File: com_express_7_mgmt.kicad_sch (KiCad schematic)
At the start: 40 parts, among them J1 Plug_Bus_CE7_EPT_401-51501-51, Q1 BSS138-7-F, Q2 BSS138-7-F, SW1 SW_1-1825027-1_THT, SW2 SW_1-1825027-1_THT, U30 MAX16150A_SOT, U31 74AUP2G132, U32 TPS3840PL30DBVR, U33 74AUP2G132

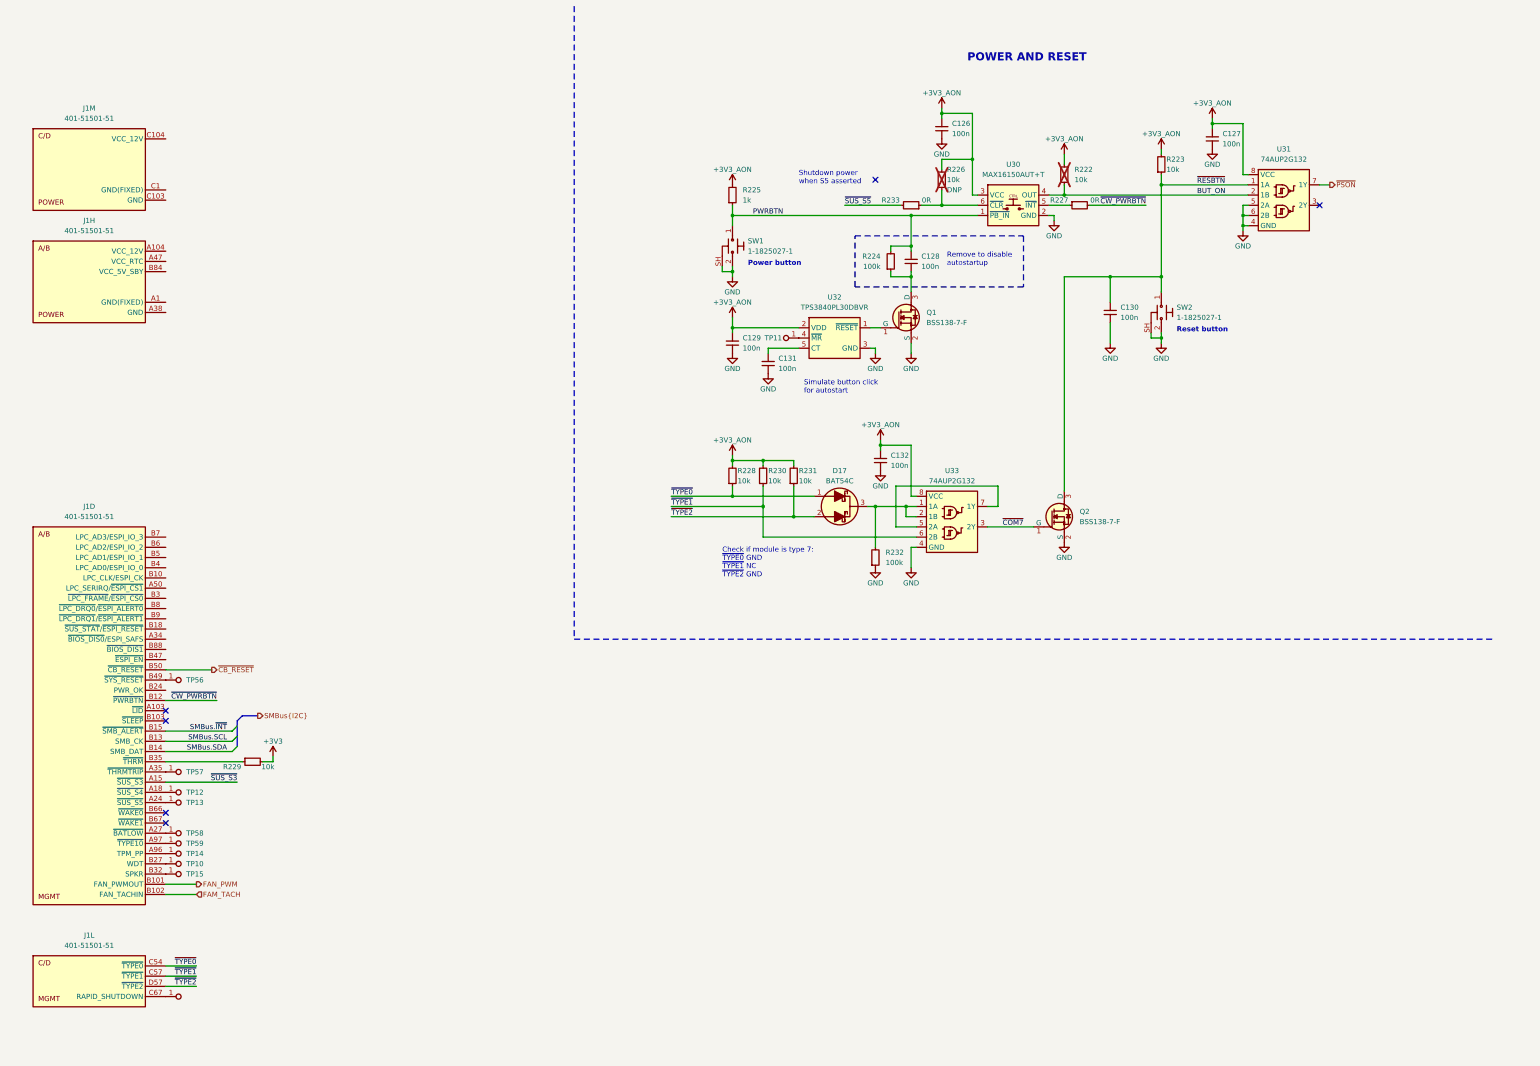
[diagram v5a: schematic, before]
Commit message: [#57905] Add MAFS carrier BIOS
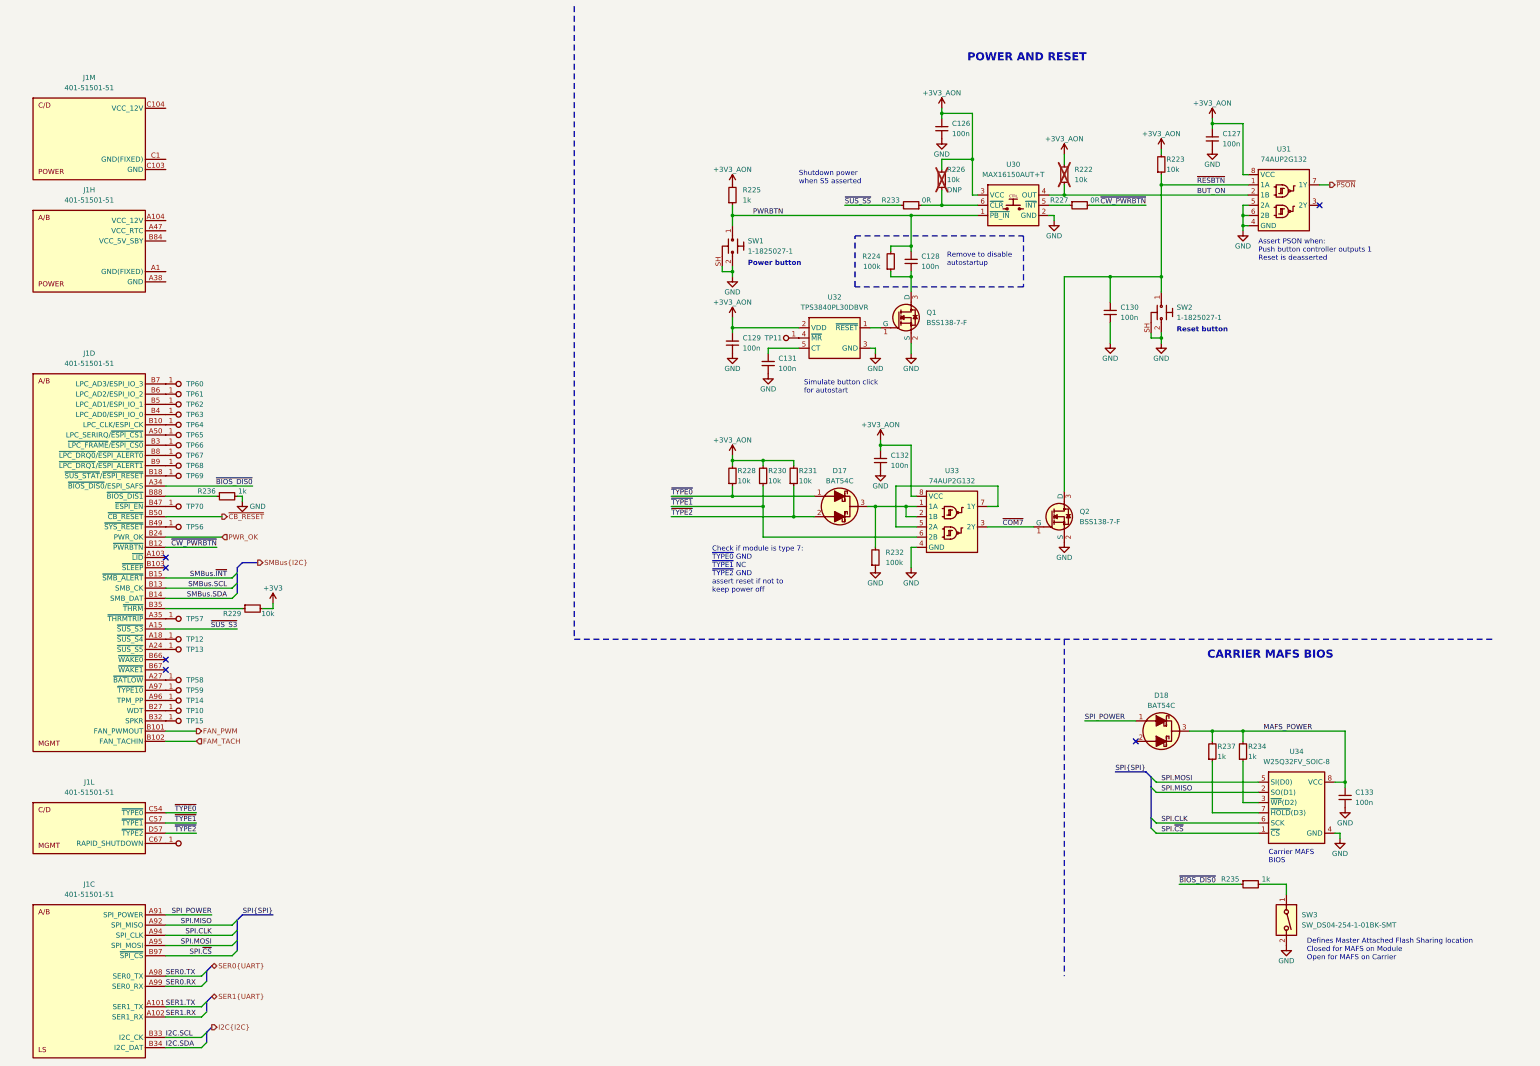
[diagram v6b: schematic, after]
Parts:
- added C133: C_100n_0402, antmicro-footprints:C_0402_1005Metric, symbol antmicroCapacitors0402:C_100n_0402
- added D18: BAT54C, antmicro-footprints:SOT-23-3, symbol antmicroDiodesRectifiersSingle:BAT54C
- added unit 3 of J1
- added R234, R235, R236, R237: R_1k_0402, antmicro-footprints:R_0402_1005Metric, symbol antmicroResistors0402:R_1k_0402
- added SW3: SW_DS04-254-1-01BK-SMT, antmicro-footprints:SW_DS04-254-1-01BK-SMT, symbol antmicroSlideSwitches:SW_DS04-254-1-01BK-SMT
- added TP60, TP61, TP62, TP63, TP64, TP65, TP66, TP67, TP68, TP69, TP70: TP_0.75mm_SMD, antmicro-footprints:TP_SMD_0.75mm, symbol antmicroTestPoints:TP_0.75mm_SMD
- added U34: W25Q32FV_SOIC-8, antmicro-footprints:SOIC-8_5.3x5.3x2mm_P1.27mm, symbol antmicroMemory:W25Q32FV_SOIC-8
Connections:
- net GND: now also C133.1, R236.2, SW3.2, U34.4 (GND)
- net ~{BIOS_DIS0}: now reaches J1.A34 (~{BIOS_DIS0}/ESPI_SAFS)
- net ~{BIOS_DIS0}: now also R235.1
- net at J1.A50 (LPC_SERIRQ/~{ESPI_CS1}): now also TP65.1
- net at J1.B10 (LPC_CLK/ESPI_CK): now also TP64.1
- net at J1.B18 (~{SUS_STAT}/~{ESPI_RESET}): now also TP69.1
- net PWR_OK: now reaches J1.B24 (PWR_OK)
- net at J1.B3 (~{LPC_FRAME}/~{ESPI_CS0}): now also TP66.1
- net at J1.B4 (LPC_AD0/ESPI_IO_0): now also TP63.1
- net at J1.B47 (~{ESPI_EN}): now also TP70.1
- net at J1.B5 (LPC_AD1/ESPI_IO_1): now also TP62.1
- net at J1.B6 (LPC_AD2/ESPI_IO_2): now also TP61.1
- net at J1.B7 (LPC_AD3/ESPI_IO_3): now also TP60.1
- net at J1.B8 (~{LPC_DRQ0}/~{ESPI_ALERT0}): now also TP67.1
- net at J1.B88 (~{BIOS_DIS1}): now also R236.1
- net at J1.B9 (~{LPC_DRQ1}/~{ESPI_ALERT1}): now also TP68.1
- new net: R234.1, U34.3 (~{WP}(D2))
- new net: R237.1, U34.7 (~{HOLD}(D3))
- new net: R235.2, SW3.1
- new net I2C.SCL: J1.B33 (I2C_CK)
- new net I2C.SDA: J1.B34 (I2C_DAT)
- new net MAFS_POWER: C133.2, D18.3, R234.2, R237.2, U34.8 (VCC)
- new net SER0.RX: J1.A99 (SER0_RX)
- new net SER0.TX: J1.A98 (SER0_TX)
- new net SER1.RX: J1.A102 (SER1_RX)
- new net SER1.TX: J1.A101 (SER1_TX)
- new net SPI.CLK: J1.A94 (SPI_CLK), U34.6 (SCK)
- new net SPI.MISO: J1.A92 (SPI_MISO), U34.2 (SO(D1))
- new net SPI.MOSI: J1.A95 (SPI_MOSI), U34.5 (SI(D0))
- new net SPI.~{CS}: J1.B97 (~{SPI_CS}), U34.1 (~{CS})
- new net SPI_POWER: D18.1, J1.A91 (SPI_POWER)
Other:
- note added: "Assert PSON when: Push button controller outputs 1 Reset is deasserted"
- note added: "CARRIER MAFS BIOS"
- note added: "Carrier MAFS BIOS"
- note added: "Check if module is type 7: ~{TYPE0} GND ~{TYPE1} NC ~{TYPE2} GND assert reset if not to keep power off"
- note added: "Defines Master Attached Flash Sharing location Closed for MAFS on Module Open for MAFS on Carrier"
- note removed: "Check if module is type 7: ~{TYPE0} GND ~{TYPE1} NC ~{TYPE2} GND"
- moved on the sheet: J1D, J1H, J1L, J1M, R229, TP10, TP12, TP13, TP14, TP15, TP56, TP57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

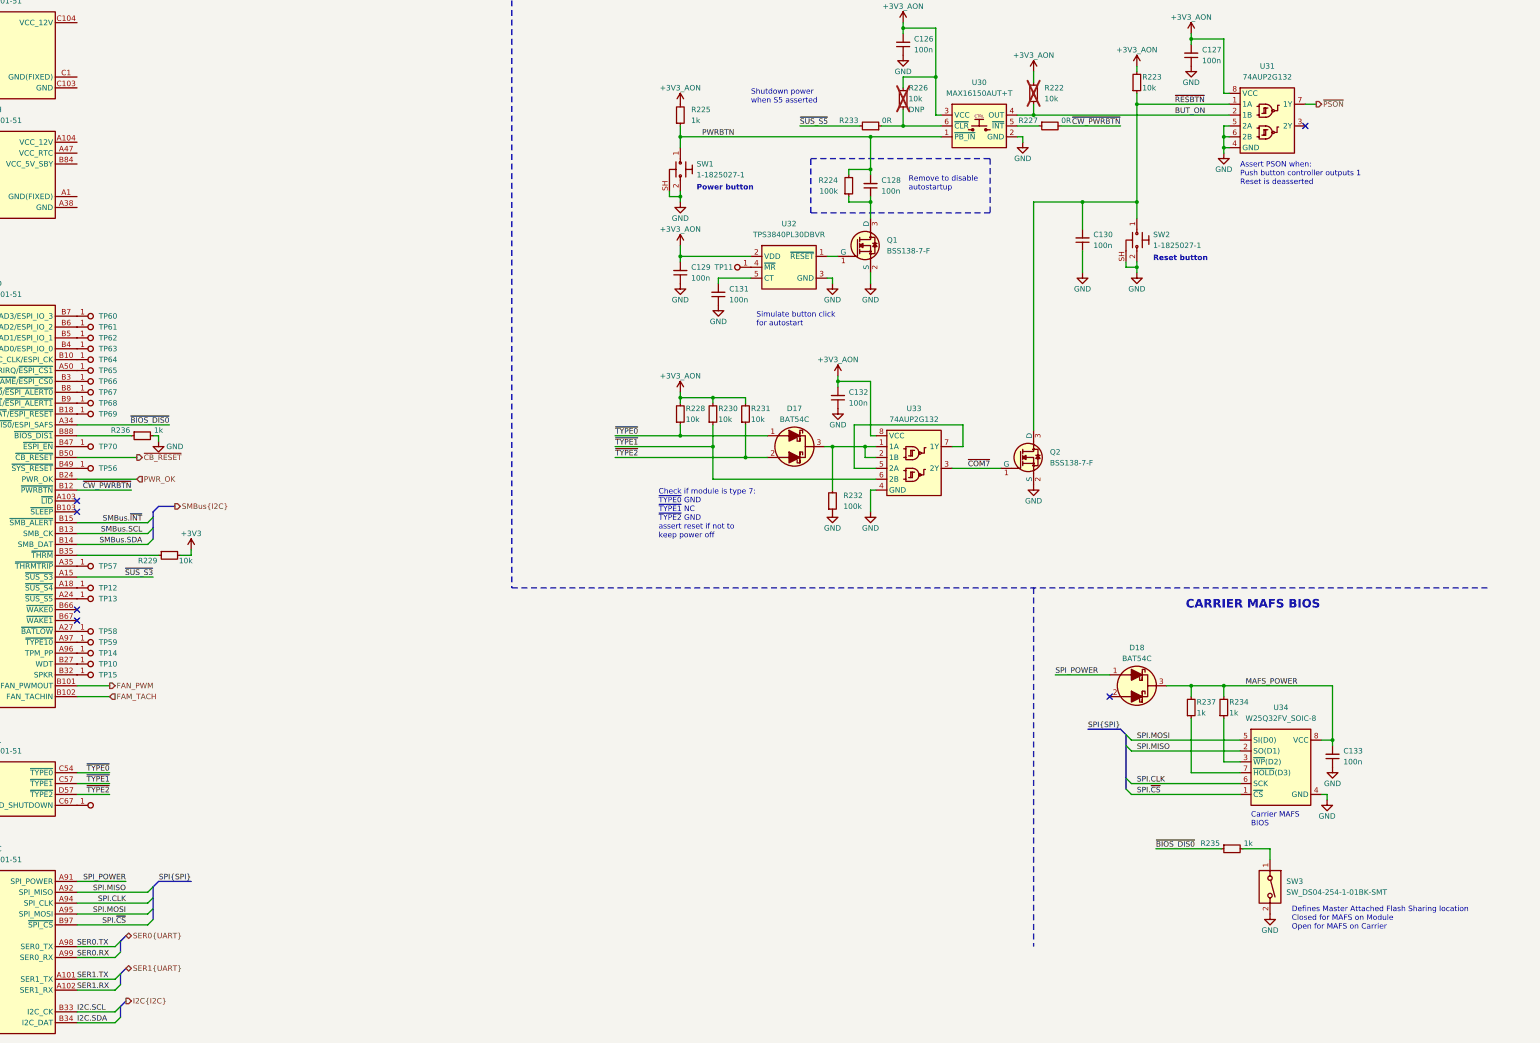
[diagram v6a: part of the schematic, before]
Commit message: [#57905] Add carrier board EEPROM
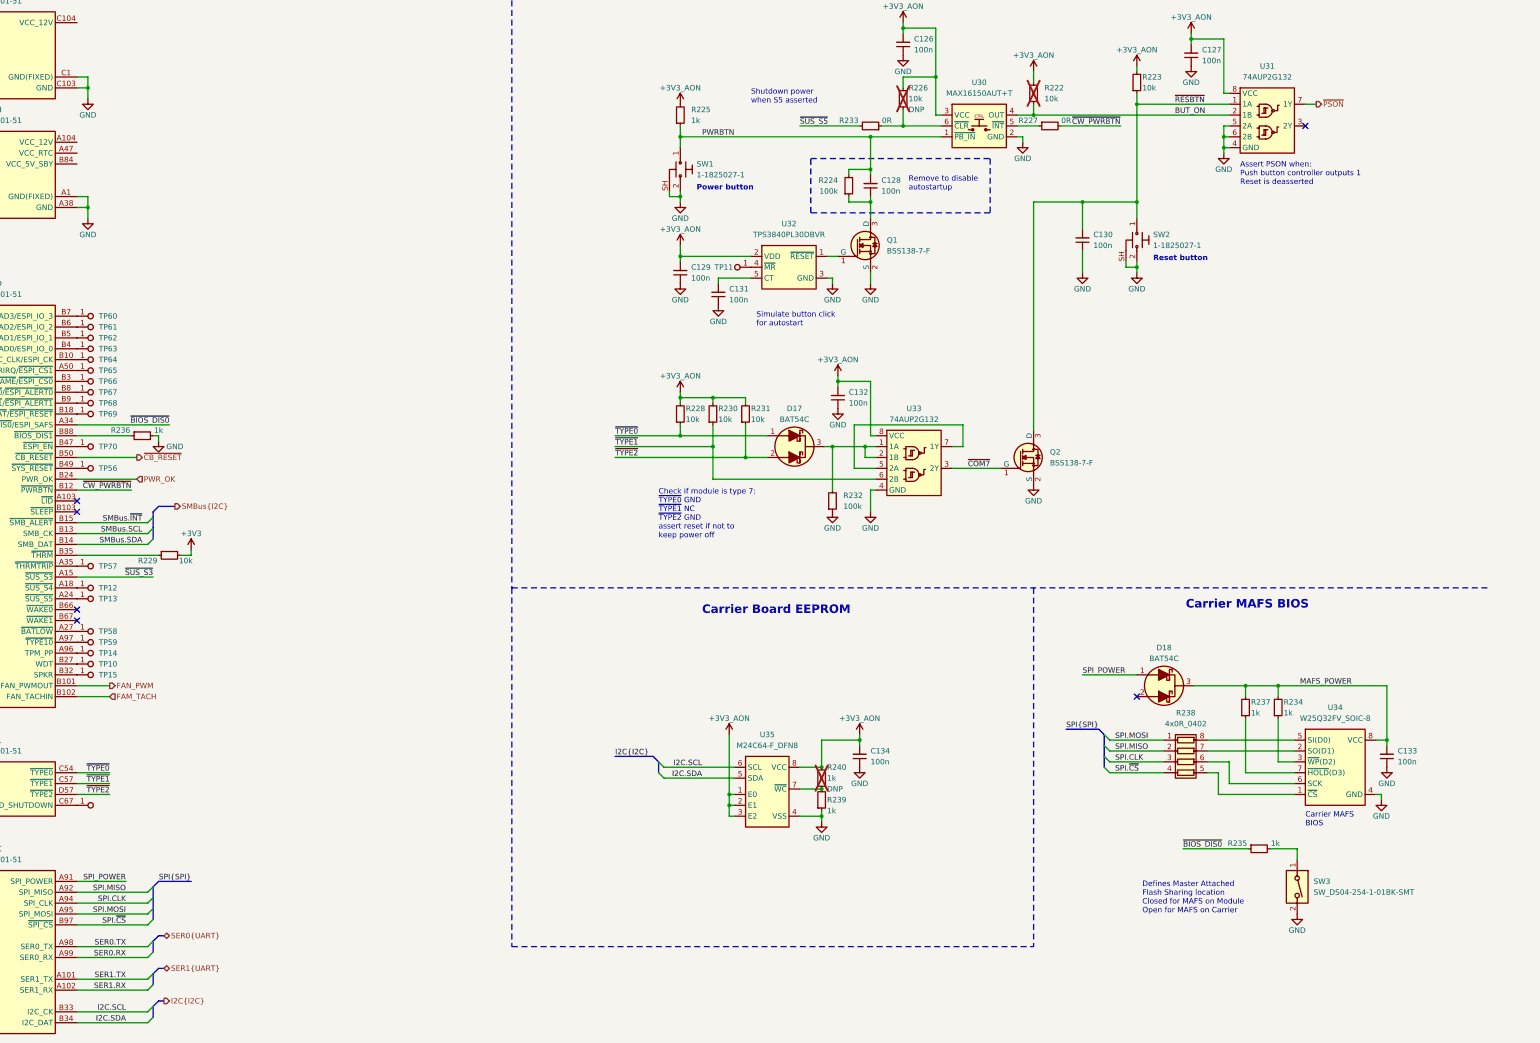
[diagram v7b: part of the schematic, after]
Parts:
- added C134: C_100n_0402, antmicro-footprints:C_0402_1005Metric, symbol antmicroCapacitors0402:C_100n_0402
- added R238: 4x0R_0402_array, antmicro-footprints:4x0R_0402_array_EXB28V, symbol antmicroResistorNetworksArrays:4x0R_0402_array
- added R239, R240: R_1k_0402, antmicro-footprints:R_0402_1005Metric, symbol antmicroResistors0402:R_1k_0402
- added U35: M24C64-F_DFN8, antmicro-footprints:DFN-8-1EP_3x2mm_P0.5mm_EP1.36x1.46mm, symbol antmicroMemory:M24C64-F_DFN8
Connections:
- net +3V3_AON: now also C134.2, R240.2, U35.1 (E0), U35.2 (E1), U35.3 (E2), U35.8 (VCC)
- net GND: now also J1.A1 (GND(FIXED)), J1.A100 (GND(FIXED)), J1.A11 (GND(FIXED)), J1.A110 (GND(FIXED)), J1.A21 (GND(FIXED)), J1.A31 (GND(FIXED)), J1.A38 (GND), J1.A41 (GND(FIXED)), J1.A51 (GND(FIXED)), J1.A57 (GND), J1.A60 (GND(FIXED)), J1.A66 (GND), J1.A70 (GND(FIXED)), J1.A73 (GND), J1.A76 (GND), J1.A79 (GND), J1.A80 (GND(FIXED)), J1.A83 (GND), J1.A90 (GND(FIXED)), J1.B1 (GND(FIXED)), J1.B100 (GND(FIXED)), J1.B11 (GND(FIXED)), J1.B110 (GND(FIXED)), J1.B21 (GND(FIXED)), J1.B31 (GND(FIXED)), J1.B38 (GND), J1.B41 (GND(FIXED)), J1.B51 (GND(FIXED)), J1.B60 (GND(FIXED)), J1.B70 (GND(FIXED)), J1.B73 (GND), J1.B76 (GND), J1.B79 (GND), J1.B80 (GND(FIXED)), J1.B83 (GND), J1.B90 (GND(FIXED)), J1.C1 (GND(FIXED)), J1.C100 (GND(FIXED)), J1.C103 (GND), J1.C11 (GND(FIXED)), J1.C110 (GND(FIXED)), J1.C14 (GND), J1.C18 (GND), J1.C2 (GND), J1.C21 (GND(FIXED)), J1.C25 (GND), J1.C28 (GND), J1.C31 (GND(FIXED)), J1.C41 (GND(FIXED)), J1.C44 (GND), J1.C48 (GND), J1.C5 (GND), J1.C51 (GND(FIXED)), J1.C60 (GND(FIXED)), J1.C70 (GND(FIXED)), J1.C73 (GND), J1.C76 (GND), J1.C8 (GND), J1.C80 (GND(FIXED)), J1.C84 (GND), J1.C87 (GND), J1.C90 (GND(FIXED)), J1.C93 (GND), J1.C96 (GND), J1.D1 (GND(FIXED)), J1.D100 (GND(FIXED)), J1.D103 (GND), J1.D11 (GND(FIXED)), J1.D110 (GND(FIXED)), J1.D14 (GND), J1.D18 (GND), J1.D2 (GND), J1.D21 (GND(FIXED)), J1.D25 (GND), J1.D28 (GND), J1.D31 (GND(FIXED)), J1.D41 (GND(FIXED)), J1.D44 (GND), J1.D48 (GND), J1.D5 (GND), J1.D51 (GND(FIXED)), J1.D60 (GND(FIXED)), J1.D67 (GND), J1.D70 (GND(FIXED)), J1.D73 (GND), J1.D76 (GND), J1.D8 (GND), J1.D80 (GND(FIXED)), J1.D84 (GND), J1.D87 (GND), J1.D90 (GND(FIXED)), J1.D93 (GND), J1.D96 (GND), C134.1, R239.1, U35.4 (VSS), U35.9 (VSS)
- net I2C.SCL: now also U35.6 (SCL)
- net I2C.SDA: now also U35.5 (SDA)
- net SPI.CLK: now also R238.3 (R3.1); no longer U34.6 (SCK)
- net SPI.MISO: now also R238.2 (R2.1); no longer U34.2 (SO(D1))
- net SPI.MOSI: now also R238.1 (R1.1); no longer U34.5 (SI(D0))
- net SPI.~{CS}: now also R238.4 (R4.1); no longer U34.1 (~{CS})
- new net: R238.5 (R4.2), U34.1 (~{CS})
- new net: R238.7 (R2.2), U34.2 (SO(D1))
- new net: R238.8 (R1.2), U34.5 (SI(D0))
- new net: R238.6 (R3.2), U34.6 (SCK)
- new net: R239.2, R240.1, U35.7 (~{WC})
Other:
- note added: "Carrier Board EEPROM"
- note removed: "CARRIER MAFS BIOS"
- moved on the sheet: C133, D18, R234, R235, R237, SW3, U34
